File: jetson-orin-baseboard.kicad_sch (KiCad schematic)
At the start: 4 parts

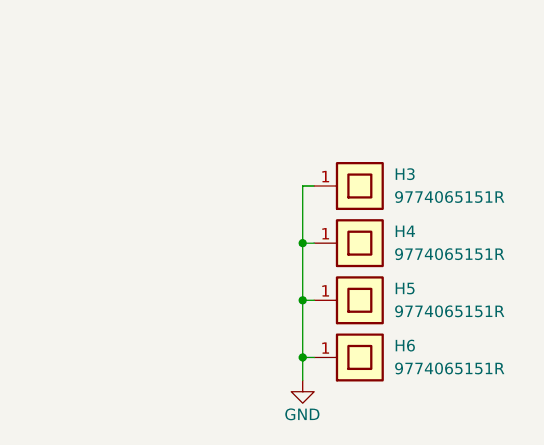
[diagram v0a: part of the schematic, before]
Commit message: Schematic Cleanup, Complete routing
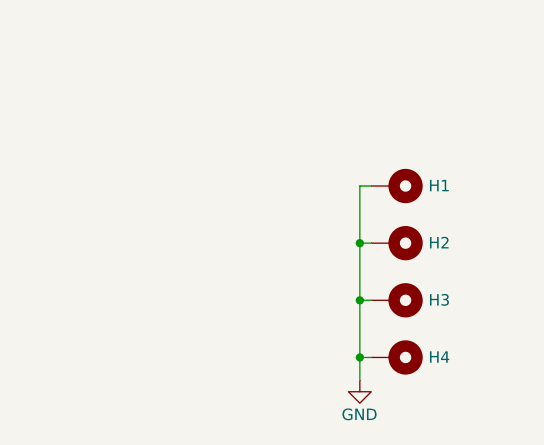
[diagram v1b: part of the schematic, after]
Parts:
- H1: renamed from H3; footprint mainboard:MountingHole2 -> JetsonCarrier:MountingHole2; symbol antmicroMechanicalParts:Spacer_Drill3.7mm_H6.5mm_9774065151R -> Mechanical:MountingHole_Pad; now left out of the parts list
- H2: renamed from H4; footprint mainboard:MountingHole2 -> JetsonCarrier:MountingHole2; symbol antmicroMechanicalParts:Spacer_Drill3.7mm_H6.5mm_9774065151R -> Mechanical:MountingHole_Pad; now left out of the parts list
- H3: renamed from H5; footprint mainboard:MountingHole2 -> JetsonCarrier:MountingHole2; symbol antmicroMechanicalParts:Spacer_Drill3.7mm_H6.5mm_9774065151R -> Mechanical:MountingHole_Pad; now left out of the parts list
- H4: renamed from H6; footprint mainboard:MountingHole2 -> JetsonCarrier:MountingHole2; symbol antmicroMechanicalParts:Spacer_Drill3.7mm_H6.5mm_9774065151R -> Mechanical:MountingHole_Pad; now left out of the parts list
